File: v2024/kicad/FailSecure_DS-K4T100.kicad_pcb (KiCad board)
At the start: 4 copper layers, 95.8 x 79 mm, 72 parts, among them CN1 WJ2EDGRC-5.08-2P, CN2 WJ2EDGRC-5.08-2P, CN3 WJ2EDGRC-5.08-8P, CN4 WAFER-200W-4A, CN5 WJ2EDGRC-5.08-2P, CN6 WAFER-200W-4A, CN7 WJ2EDGRC-5.08-2P, Q1 BSS138, Q2 BSS138, SW1 1TS002B-2300-4301, SW2 1TS002B-2300-4301, U1 PicoW, U2 TPS563200DDCR, U3 BX-DS2.54-4PTP, U4 SFH6206-3T

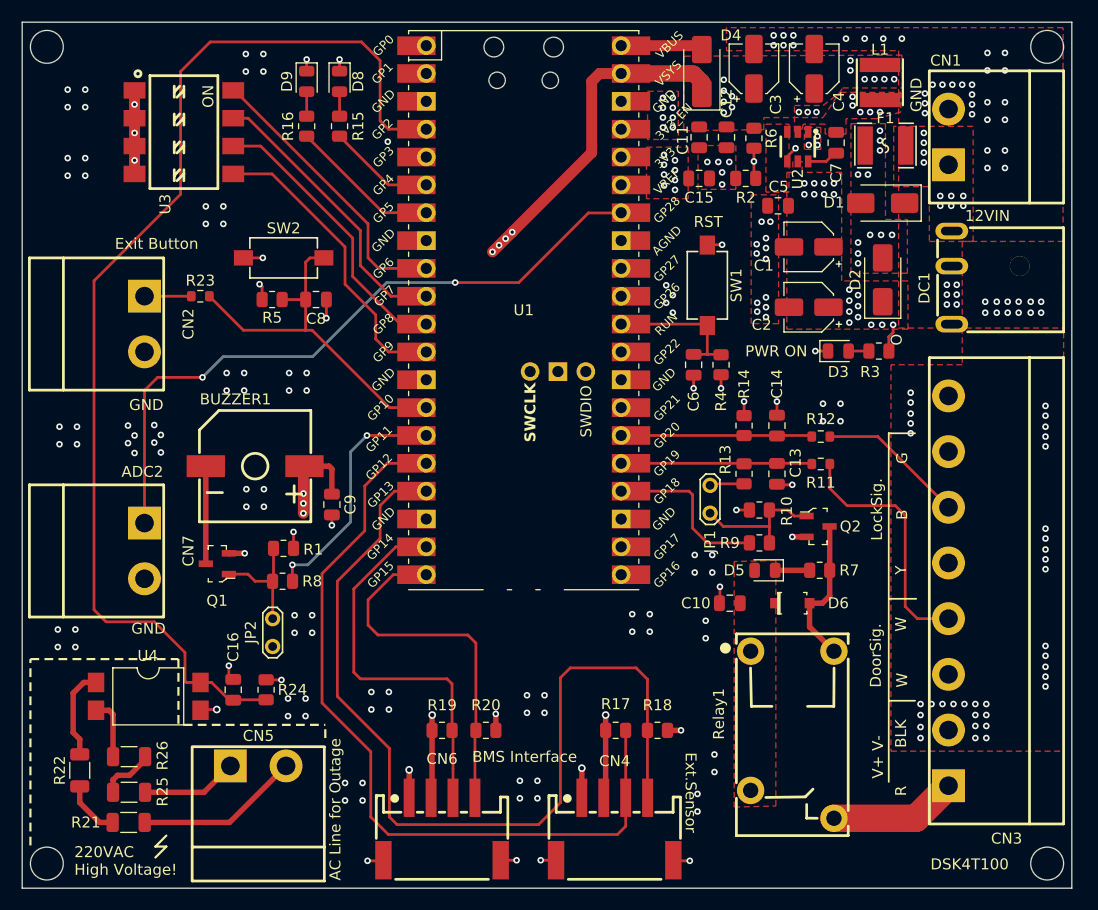
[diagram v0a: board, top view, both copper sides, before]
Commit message: Kicad, update PCB layout for a new schematic
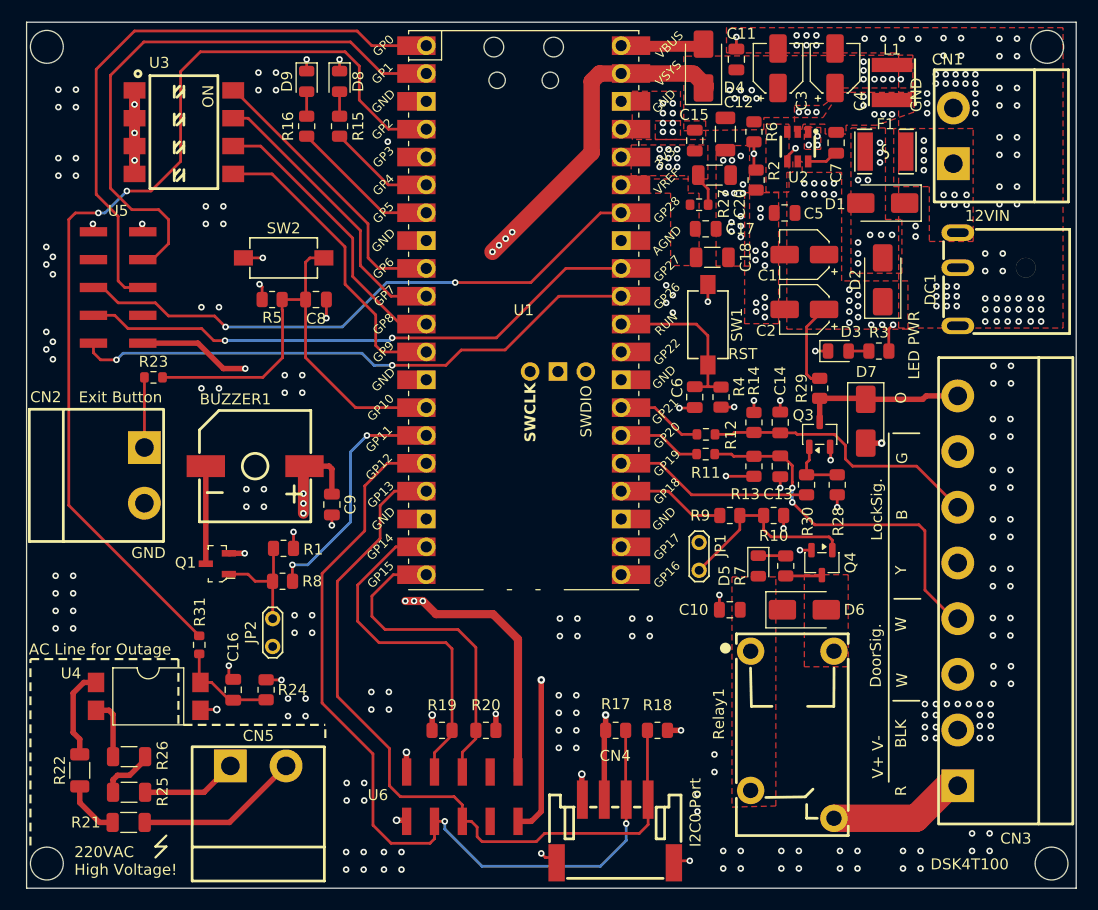
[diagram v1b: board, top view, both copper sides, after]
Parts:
- removed CN6: WAFER-200W-4A, WAFER-200W-4A:CONN-SMD_4P-P2.00_HANBO_WAFER-200W-4A
- removed CN7: WJ2EDGRC-5.08-2P, WJ2EDGRC-5.08-2P:CONN-TH_2P-P5.08_WJ2EDGRC-5.08-2P
- removed Q2: BSS138, digikey-footprints:SOT-23-3
- added C17: 0.1u, Capacitor_SMD:C_0805_2012Metric, F.Cu at (159.6, 83.8)
- added C18: 1u, Capacitor_SMD:C_1206_3216Metric, F.Cu at (160.2, 86.5)
- added C20: 1u, Capacitor_SMD:C_1206_3216Metric, F.Cu at (160.4, 79.0)
- added D7: SMAJ26A, Diode_SMD:D_SMA, F.Cu at (174.2, 101.4)
- added Q3: BSS138, Package_TO_SOT_SMD:SOT-23-3, F.Cu at (170.0, 102.6)
- added Q4: BSS138, Package_TO_SOT_SMD:SOT-23-3, F.Cu at (170.2, 114.3)
- added R27: 0R, Resistor_SMD:R_0603_1608Metric, F.Cu at (159.0, 81.7)
- added R28: 10k, Resistor_SMD:R_0805_2012Metric, F.Cu at (171.6, 107.2)
- added R29: 10k, Resistor_SMD:R_0805_2012Metric, F.Cu at (170.0, 98.4)
- added R30: 100R, Resistor_SMD:R_0805_2012Metric, F.Cu at (168.8, 107.2)
- added R31: 0R, Resistor_SMD:R_0603_1608Metric, F.Cu at (113.4, 121.8)
- added U5: HX PM2.54-2X5P WT, HX_PM2.54-2x5P_WT:HDR-SMD_10P-P2.54-H-F-R2-C5-W8.5, F.Cu at (106.0, 89.2)
- added U6: HX PM2.54-2X5P WT, HX_PM2.54-2x5P_WT:HDR-SMD_10P-P2.54-H-F-R2-C5-W8.5, F.Cu at (137.4, 135.7)
- C12: value 0.1u -> 1u; footprint Capacitor_SMD:C_0805_2012Metric -> Capacitor_SMD:C_1206_3216Metric
- CN4: value WAFER-200W-4A -> WAFER-200W-4P; footprint WAFER-200W-4A:CONN-SMD_4P-P2.00_HANBO_WAFER-200W-4A -> WAFER-200W-4P:CONN-SMD_WAFER-200W-4P
- D6: value 1N4148W-TP -> SMAJ26A; footprint digikey-footprints:SOD-123 -> Diode_SMD:D_SMA
- moved CN2 13.8 mm to (108.4, 106.3)
- moved R11 10.5 mm to (159.6, 104.4)
- moved R12 10.5 mm to (159.6, 102.6)
- moved R23 8.55 mm to (109.2, 97.4)
- moved C11 7.87 mm to (162.4, 68.4), turned to -90 degrees
- moved JP1 5.31 mm to (159.0, 112.5)
- moved R9 3.68 mm to (161.8, 110.0)
- moved SW1 3.60 mm to (159.8, 92.6)
- moved C15 3.47 mm to (158.6, 75.8), turned to -90 degrees
- moved R7 3.13 mm to (166.9, 114.6), turned to 90 degrees
- moved C6 2.95 mm to (158.6, 99.2)
- moved R4 2.95 mm to (161.0, 99.2)
- moved C3 2.20 mm to (166.2, 69.2)
- moved C4 1.90 mm to (171.4, 69.2)
- moved R10 1.39 mm to (165.8, 110.0), turned to 180 degrees
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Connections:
- net /DO_DoorLock renamed /DO_DoorLock_PWR
- net Net-(CN3-Pad1) renamed V_DSK4T100
- C12 pad 1: GND -> +5V
- C12 pad 2: +5V -> GND
- C13 pad 2: /DI_DoorStatus -> /DSK4T100_DoorStatus
- C14 pad 2: /DI_LockStatus -> /DSK4T100_LockStatus
- C16 pad 2: /DI_ZeroCross -> Net-(C16-Pad2)
- CN3 pad 8: unconnected-(CN3-Pad8) -> /DSK4T100_Open
- R11 pad 2: /DI_DoorStatus -> /DI_DoorLock_DoorStatus
- R12 pad 2: /DI_LockStatus -> /DI_DoorLock_LockStatus
- R13 pad 1: /DI_DoorStatus -> /DSK4T100_DoorStatus
- R14 pad 1: /DI_LockStatus -> /DSK4T100_LockStatus
- R24 pad 1: /DI_ZeroCross -> Net-(C16-Pad2)
- R7 pad 1: Net-(Q2-D) -> Net-(D6-A2)
- Relay1 pad 2: Net-(Q2-D) -> Net-(D6-A2)
- U1 pad 1: unconnected-(U1-GPIO0-Pad1) -> /DO_GPIO0
- U1 pad 2: unconnected-(U1-GPIO1-Pad2) -> /DO_GPIO1
- U1 pad 25: /DI_DoorStatus -> /DO_DoorLock_Open
- U1 pad 26: /DI_LockStatus -> /DI_DoorLock_DoorStatus
- U1 pad 27: unconnected-(U1-GPIO21-Pad27)_1 -> /DI_DoorLock_LockStatus
- U1 pad 31: unconnected-(U1-GPIO26_ADC0-Pad31) -> /AIN_ADC0
- U1 pad 32: unconnected-(U1-GPIO27_ADC1-Pad32)_1 -> /AIN_ADC1
- U1 pad 35: unconnected-(U1-ADC_VREF-Pad35)_1 -> /ADC_VREF
- U4 pad 4: /DI_ZeroCross -> Net-(C16-Pad2)
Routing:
- net /DO_GPIO0: track 0.00 -> 54.7 mm
- net /DO_GPIO1: track 0.00 -> 53.2 mm
- net /AIN_ADC0: track 0.00 -> 52.6 mm, vias 0 -> 2
- net /AIN_ADC1: track 0.00 -> 51.8 mm, vias 0 -> 2
- net +5V: track 94.4 -> 141.9 mm, vias 19 -> 24
- net +3.3V: track 227.0 -> 247.9 mm, vias 16 -> 19
- net /DO_DoorLock_Open: track 0.00 -> 18.1 mm
- net /DI_LockStatus: track 17.4 -> 0.00 mm
- net /DI_DoorStatus: track 17.4 -> 0.00 mm
- net VIN: track 84.0 -> 68.3 mm
- net /DSK4T100_Open: track 0.00 -> 14.9 mm
- net /I2C0_SCL: track 84.4 -> 70.1 mm
- net Net-(Q2-D): track 13.8 -> 0.00 mm
- net /DSK4T100_LockStatus: track 13.5 -> 25.8 mm
- net /DI_ZeroCross: track 103.0 -> 91.4 mm, vias 0 -> 2
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- added copper zone on F.Cu, net /ADC_VREF
- added copper zone on F.Cu, net Net-(D6-A2)
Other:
- outline, holes or cut-outs redrawn
- board text added: "I2C0 Port"
- board text added: "LED PWR"
- board text removed: "ADC2"
- board text removed: "BMS Interface"
- board text removed: "Ext.Sensor"
- board text removed: "PWR ON"

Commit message: Kicad, move 2x5 connector to fit inside the board
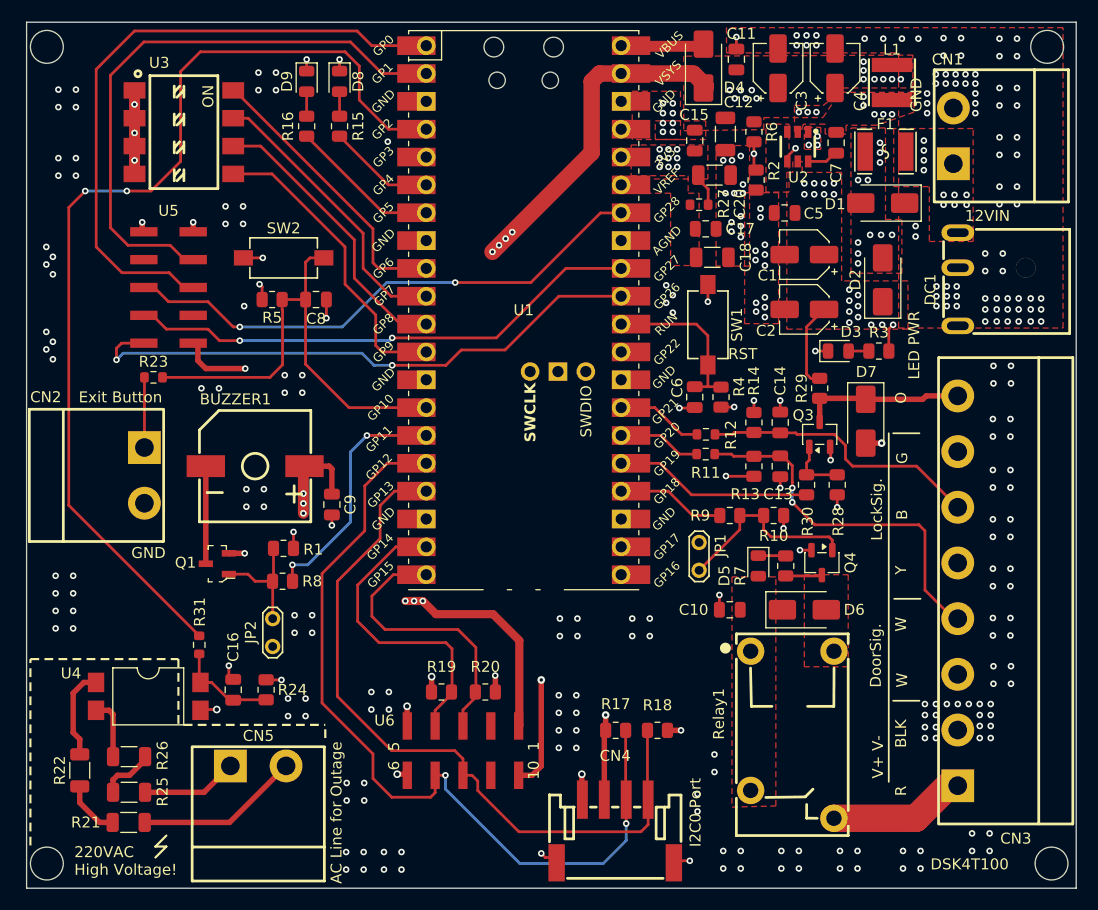
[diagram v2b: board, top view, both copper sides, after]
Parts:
- moved U5 4.60 mm to (110.6, 89.2)
- moved U6 4.20 mm to (137.5, 131.4)
- moved R19 3.50 mm to (135.5, 126.1)
- moved R20 3.50 mm to (139.5, 126.1)
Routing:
- net +3.3V: track 247.9 -> 238.9 mm
- net +5V: track 141.9 -> 133.6 mm
- net /AIN_ADC1: track 51.8 -> 47.2 mm
- net /AIN_ADC2: track 53.9 -> 49.3 mm
- net /I2C1_SDA: track 32.7 -> 28.3 mm
- net /I2C1_SCL: track 30.3 -> 25.9 mm
- net /DO_GPIO0: track 54.7 -> 58.7 mm
- net /I2C0_SCL: track 70.1 -> 67.3 mm
- net /I2C0_SDA: track 79.5 -> 77.1 mm
- net /DI_ExitButton: track 42.7 -> 43.4 mm
- net /DO_GPIO1: track 53.2 -> 53.9 mm
- net /DI_ZeroCross: track 91.4 -> 92.0 mm
- net /AIN_ADC0: track 52.6 -> 53.1 mm
- net GND: track 45.0 -> 45.3 mm, vias 305 -> 304
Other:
- board text added: "10 1"
- board text added: "6 5"
